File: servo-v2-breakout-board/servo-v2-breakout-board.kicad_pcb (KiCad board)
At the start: 2 copper layers, 18.5 x 94.5 mm, 3 parts, among them J1 AXK850145WG

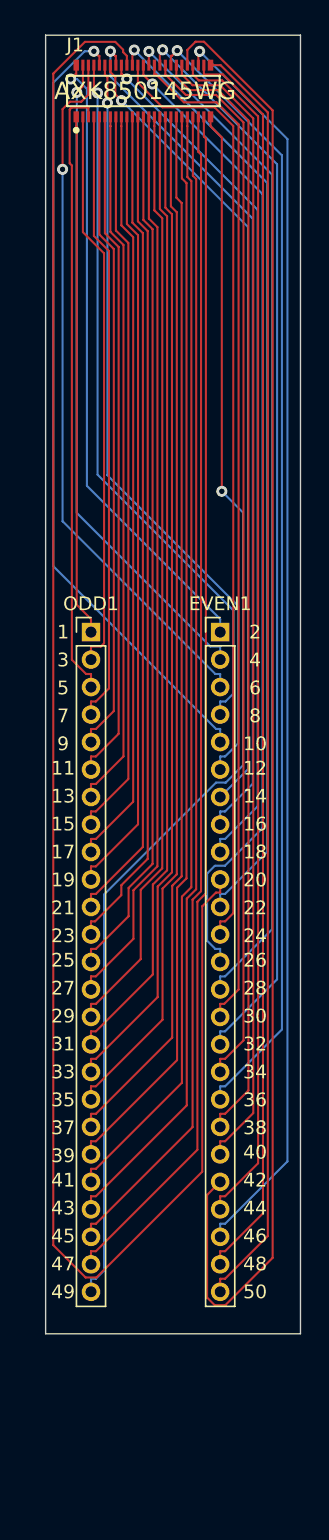
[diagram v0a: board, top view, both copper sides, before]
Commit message: corrected pin numbering, which was mirrored on v1. changed headers to standard size
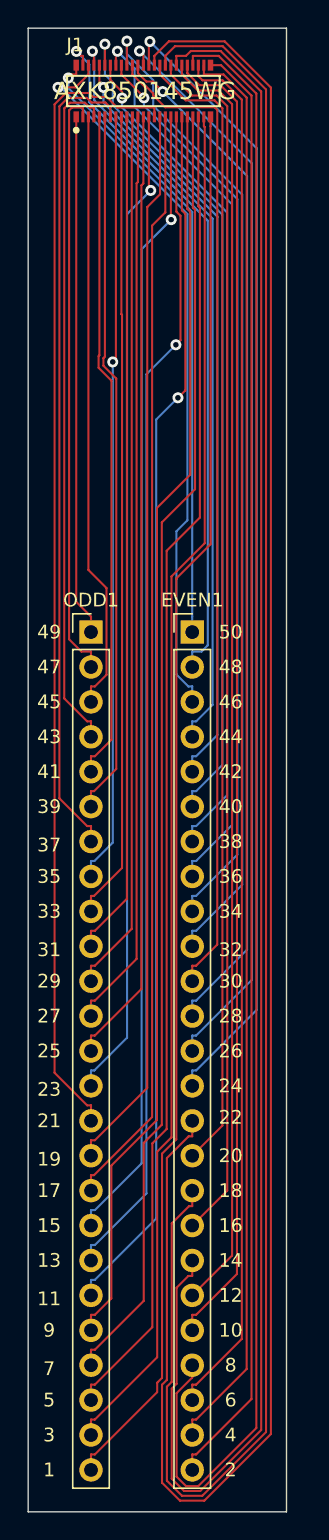
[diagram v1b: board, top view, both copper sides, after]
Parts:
- EVEN1, ODD1: footprint Connector_PinHeader_2.00mm:PinHeader_1x25_P2.00mm_Vertical -> Connector_PinHeader_2.54mm:PinHeader_1x25_P2.54mm_Vertical
- moved EVEN1 2.03 mm to (136.9, 57.1)
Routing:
- net Net-(EVEN1-Pad15): track 74.0 -> 146.8 mm
- net Net-(EVEN1-Pad17): track 77.8 -> 138.9 mm
- net Net-(EVEN1-Pad10): track 129.7 -> 72.8 mm, vias 0 -> 1
- net Net-(EVEN1-Pad19): track 81.7 -> 131.0 mm
- net Net-(EVEN1-Pad22): track 87.6 -> 119.9 mm
- net Net-(J1-Pad29): track 68.1 -> 83.9 mm
- net Net-(EVEN1-Pad25): track 93.1 -> 105.8 mm
- net Net-(EVEN1-Pad21): track 108.4 -> 96.0 mm
- net Net-(J1-Pad47): track 87.2 -> 99.5 mm
- net Net-(EVEN1-Pad24): track 91.3 -> 103.6 mm
- net Net-(J1-Pad45): track 85.1 -> 96.9 mm
- net Net-(J1-Pad43): track 83.0 -> 94.2 mm
- net Net-(J1-Pad41): track 80.8 -> 91.5 mm
- net Net-(J1-Pad49): track 91.7 -> 102.2 mm, vias 1 -> 0
- net Net-(J1-Pad39): track 78.7 -> 88.9 mm, vias 0 -> 1
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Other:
- board size 18.5 x 94.5 mm -> 18.8 x 108 mm
